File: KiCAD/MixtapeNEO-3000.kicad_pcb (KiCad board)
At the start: 2 copper layers, 99 x 64.8 mm, 51 parts, among them J1 CONN_01X04, J2 CONN_01X04, J4 Con_3-5V, J6 CONN_01X02_MALE, SW1 SW_Push, SW2 SW_Push, SW3 SW_Push, U1 ATTINY85-20SU, U2 PAM8002

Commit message: revised version and photos
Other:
- net class thinSiech added: clearance 0.2, trace_width 0.3, via_dia 0.6, via_drill 0.4
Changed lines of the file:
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@@
 (kicad_pcb (version 4) (host pcbnew 4.0.7-e0-6372~58~ubuntu16.04.1)
   (general
-    (links 111)
-    (no_connects 14)
-    (area 0 0 0 0)
+    (links 103)
+    (no_connects 6)
+    (area 92.71 54.102 202.692001 136.398001)
     (thickness 1.6)
     (drawings 0)
@@
     (add_net VCC)
   )
+  (net_class thinSiech ""
+    (clearance 0.2)
+    (trace_width 0.3)
+    (via_dia 0.6)
+    (via_drill 0.4)
+    (uvia_dia 0.3)
+    (uvia_drill 0.1)
+  )
   (module Resistors_SMD:R_0612 (layer B.Cu)

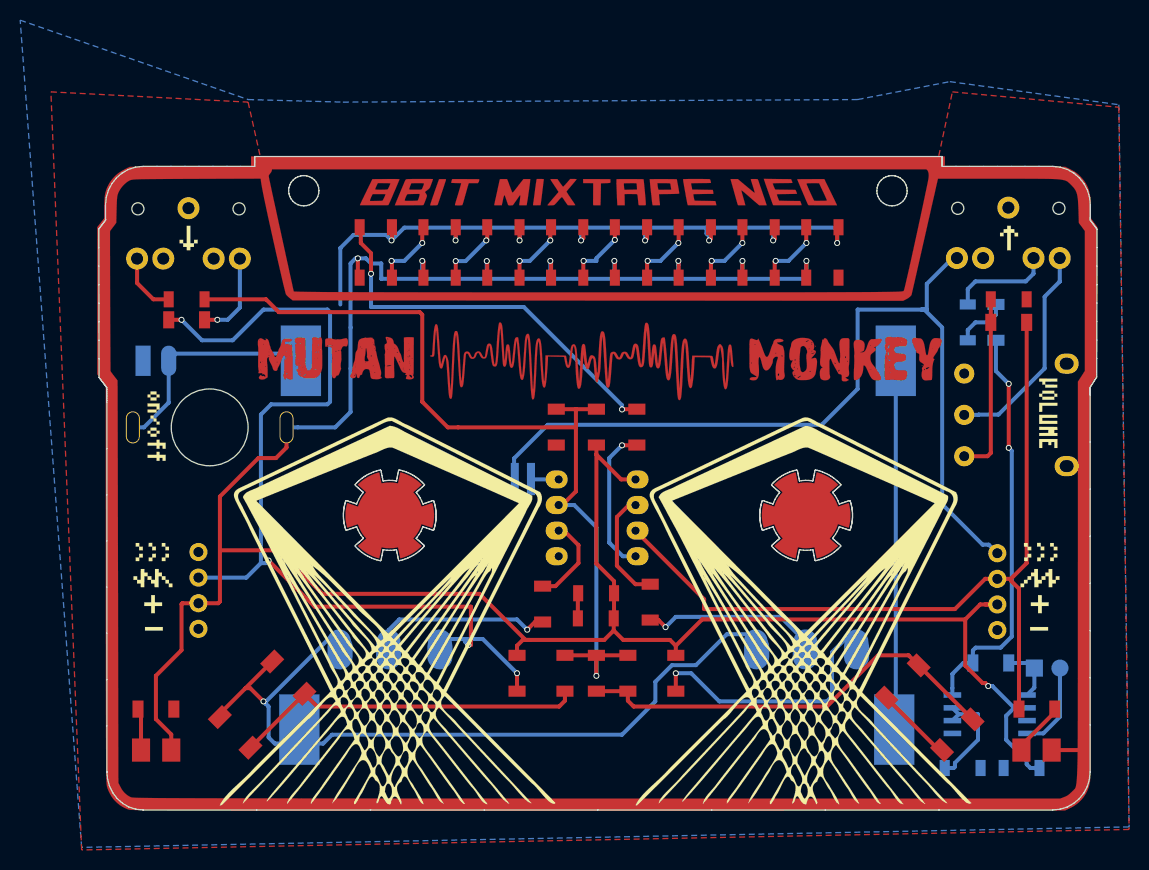
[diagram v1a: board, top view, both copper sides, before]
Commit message: fixed board v3.3, incl dimplus special
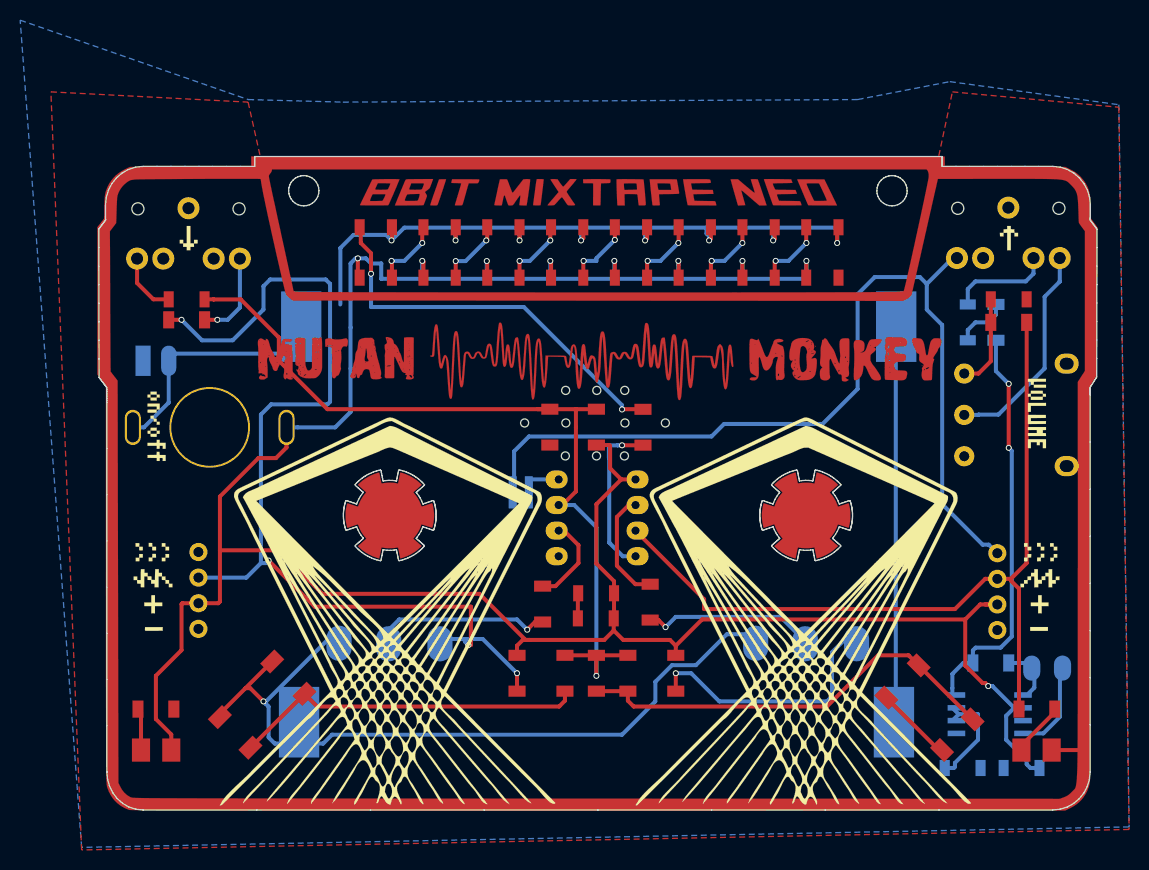
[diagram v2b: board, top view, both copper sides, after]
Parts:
- added ?: , 8BitMixtape3000-MutanMonkey:Speaker_Loch08, F.Cu at (152.7, 94.0)
- added ?: , 8BitMixtape3000-MutanMonkey:Speaker_Loch08, F.Cu at (149.9, 97.3)
- added ?: , 8BitMixtape3000-MutanMonkey:Speaker_Loch08, F.Cu at (146.8, 94.0)
- added ?: , 8BitMixtape3000-MutanMonkey:Speaker_Loch08, F.Cu at (156.7, 94.0)
- added ?: , 8BitMixtape3000-MutanMonkey:Speaker_Loch08, F.Cu at (142.7, 94.0)
- added ?: , 8BitMixtape3000-MutanMonkey:Speaker_Loch08, F.Cu at (152.7, 90.8)
- added ?: , 8BitMixtape3000-MutanMonkey:Speaker_Loch08, F.Cu at (149.9, 90.8)
- added ?: , 8BitMixtape3000-MutanMonkey:Speaker_Loch08, F.Cu at (146.8, 90.8)
- added ?: , 8BitMixtape3000-MutanMonkey:Speaker_Loch08, F.Cu at (146.8, 97.3)
- added ?: , 8BitMixtape3000-MutanMonkey:Speaker_Loch08, F.Cu at (152.6, 97.3)
- POT3-Vol1: footprint 8BitMixtape3000-MutanMonkey:Potentiometer_wheel -> 8BitMixtape-3000-V2:Potentiometer_wheel
- Speaker1: footprint 8BitMixtape3000-MutanMonkey:SpeakerPads_SMD -> 8BitMixtape-3000-V2:SpeakerPads_SMD
- U2: footprint 8BitMixtape3000-MutanMonkey:SO-8_5.3x6.2mm_Pitch1.27mm -> 8BitMixtape3000-MutanMonkey:SO-8_fixed
- board1: footprint 8BitMixtape3000-MutanMonkey:MixtapeNEO-3000 -> 8BitMixtape3000-MutanMonkey:MixtapeNEO-3000_mutanmonkey_final
- moved BT1 3.38 mm to (150.1, 84.6)
- moved J6 1.34 mm to (142.4, 100.9)
- moved BT2 0.73 mm to (149.9, 123.6)
- moved R2 0.64 mm to (145.2, 94.5)
- moved R9 0.61 mm to (154.5, 94.5)
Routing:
- net CV_OUT: track 18.0 -> 9.28 mm
- net PB3: track 89.2 -> 83.4 mm
- net CV_IN: track 94.5 -> 100.0 mm
- net Sync_OUT: track 88.0 -> 90.7 mm
- net PB0: track 14.8 -> 15.6 mm
- net VCC: track 271.5 -> 270.8 mm
